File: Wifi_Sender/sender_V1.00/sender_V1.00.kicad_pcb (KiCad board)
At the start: 2 copper layers, 2 parts, among them U1 ESP32-DevKitC, U2 Teensy4.1

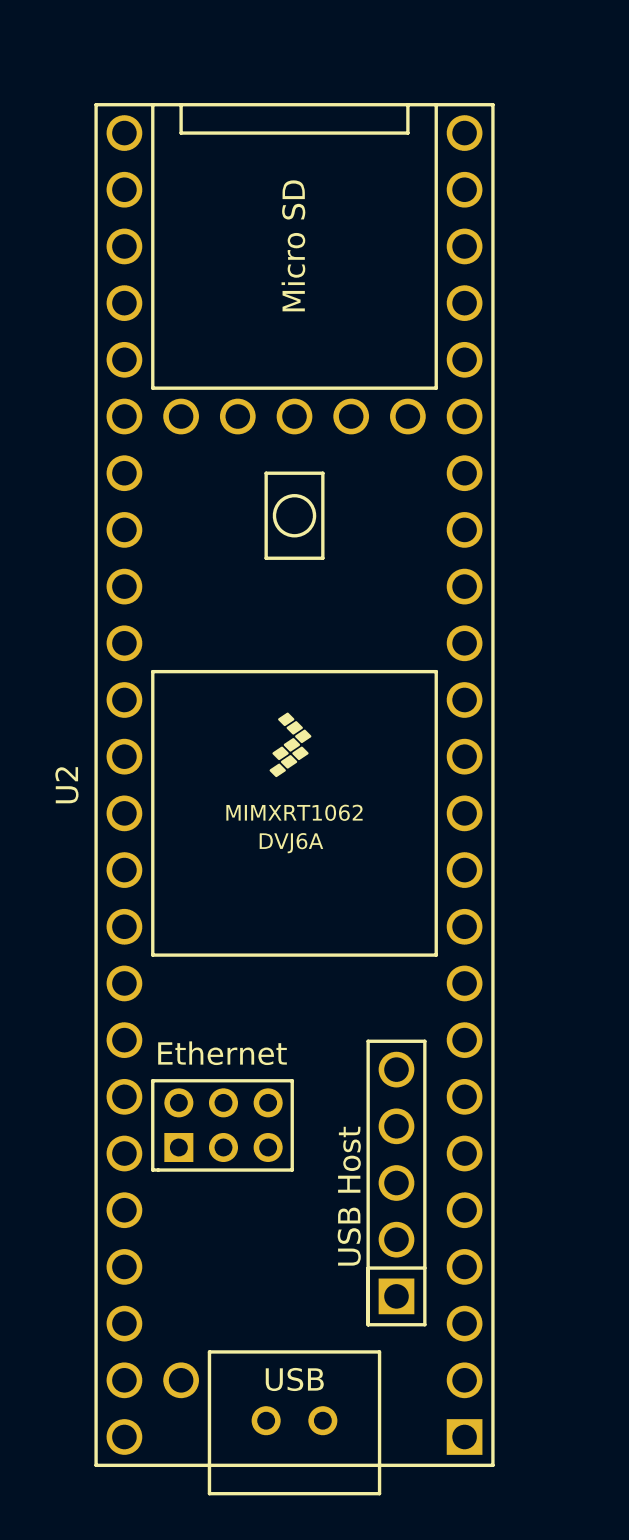
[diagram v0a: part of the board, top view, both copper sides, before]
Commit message: Removed old Pics
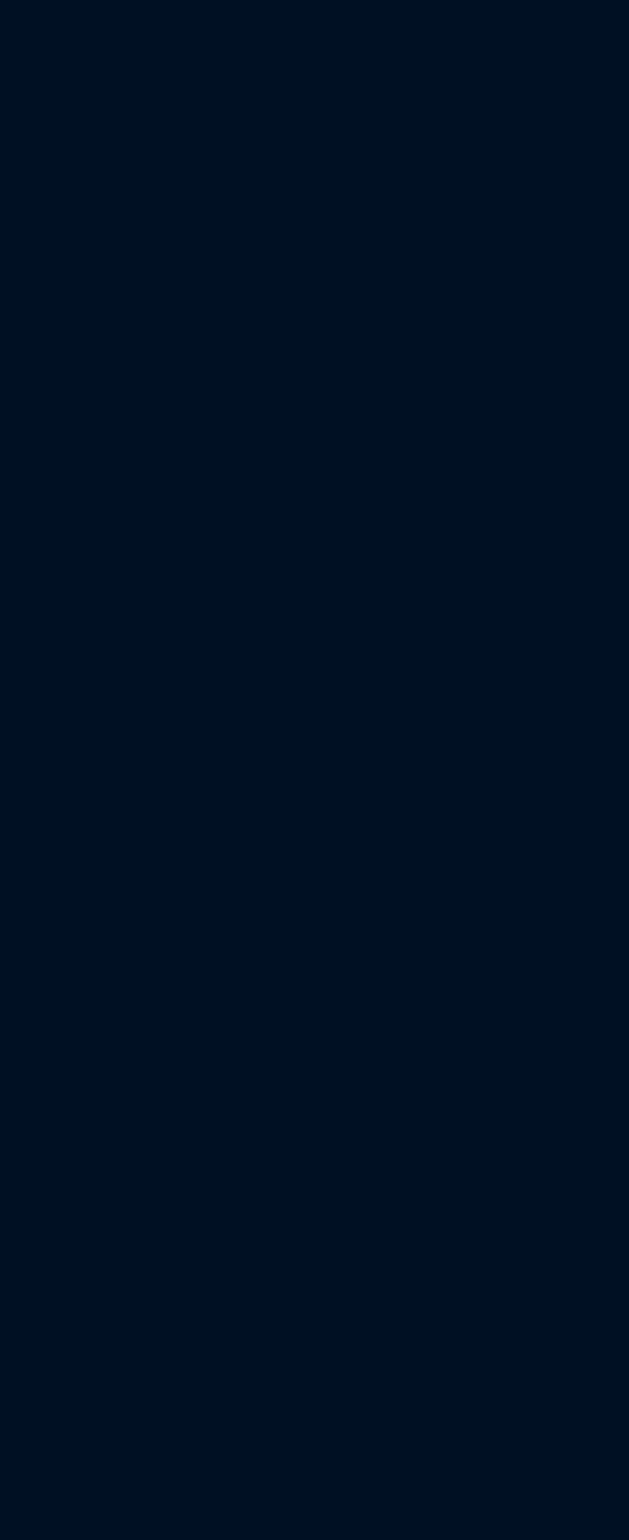
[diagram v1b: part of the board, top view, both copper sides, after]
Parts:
- removed U2: Teensy4.1, teensy:Teensy41
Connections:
- U1 pad 1: Net-(U1-Pad1) -> unconnected-(U1-Pad1)
- U1 pad 10: Net-(U1-Pad10) -> unconnected-(U1-Pad10)
- U1 pad 11: Net-(U1-Pad11) -> unconnected-(U1-Pad11)
- U1 pad 12: Net-(U1-Pad12) -> unconnected-(U1-Pad12)
- U1 pad 13: Net-(U1-Pad13) -> unconnected-(U1-Pad13)
- U1 pad 14: Net-(U1-Pad14) -> unconnected-(U1-Pad14)
- U1 pad 15: Net-(U1-Pad15) -> unconnected-(U1-Pad15)
- U1 pad 16: Net-(U1-Pad16) -> unconnected-(U1-Pad16)
- U1 pad 17: Net-(U1-Pad17) -> unconnected-(U1-Pad17)
- U1 pad 18: Net-(U1-Pad18) -> unconnected-(U1-Pad18)
- U1 pad 19: Net-(U1-Pad19) -> unconnected-(U1-Pad19)
- U1 pad 2: Net-(U1-Pad2) -> unconnected-(U1-Pad2)
- U1 pad 20: Net-(U1-Pad20) -> unconnected-(U1-Pad20)
- U1 pad 21: Net-(U1-Pad21) -> unconnected-(U1-Pad21)
- U1 pad 22: Net-(U1-Pad22) -> unconnected-(U1-Pad22)
- U1 pad 23: Net-(U1-Pad23) -> unconnected-(U1-Pad23)
- U1 pad 24: Net-(U1-Pad24) -> unconnected-(U1-Pad24)
- U1 pad 25: Net-(U1-Pad25) -> unconnected-(U1-Pad25)
- U1 pad 26: Net-(U1-Pad26) -> unconnected-(U1-Pad26)
- U1 pad 27: Net-(U1-Pad27) -> unconnected-(U1-Pad27)
- U1 pad 28: Net-(U1-Pad28) -> unconnected-(U1-Pad28)
- U1 pad 29: Net-(U1-Pad29) -> unconnected-(U1-Pad29)
- U1 pad 3: Net-(U1-Pad3) -> unconnected-(U1-Pad3)
- U1 pad 30: Net-(U1-Pad30) -> unconnected-(U1-Pad30)
- U1 pad 31: Net-(U1-Pad31) -> unconnected-(U1-Pad31)
- U1 pad 32: Net-(U1-Pad32) -> unconnected-(U1-Pad32)
- U1 pad 33: Net-(U1-Pad33) -> unconnected-(U1-Pad33)
- U1 pad 34: Net-(U1-Pad34) -> unconnected-(U1-Pad34)
- U1 pad 35: Net-(U1-Pad35) -> unconnected-(U1-Pad35)
- U1 pad 36: Net-(U1-Pad36) -> unconnected-(U1-Pad36)
- U1 pad 37: Net-(U1-Pad37) -> unconnected-(U1-Pad37)
- U1 pad 38: Net-(U1-Pad38) -> unconnected-(U1-Pad38)
- U1 pad 4: Net-(U1-Pad4) -> unconnected-(U1-Pad4)
- U1 pad 5: Net-(U1-Pad5) -> unconnected-(U1-Pad5)
- U1 pad 6: Net-(U1-Pad6) -> unconnected-(U1-Pad6)
- U1 pad 7: Net-(U1-Pad7) -> unconnected-(U1-Pad7)
- U1 pad 8: Net-(U1-Pad8) -> unconnected-(U1-Pad8)
- U1 pad 9: Net-(U1-Pad9) -> unconnected-(U1-Pad9)
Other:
- net class Default removed

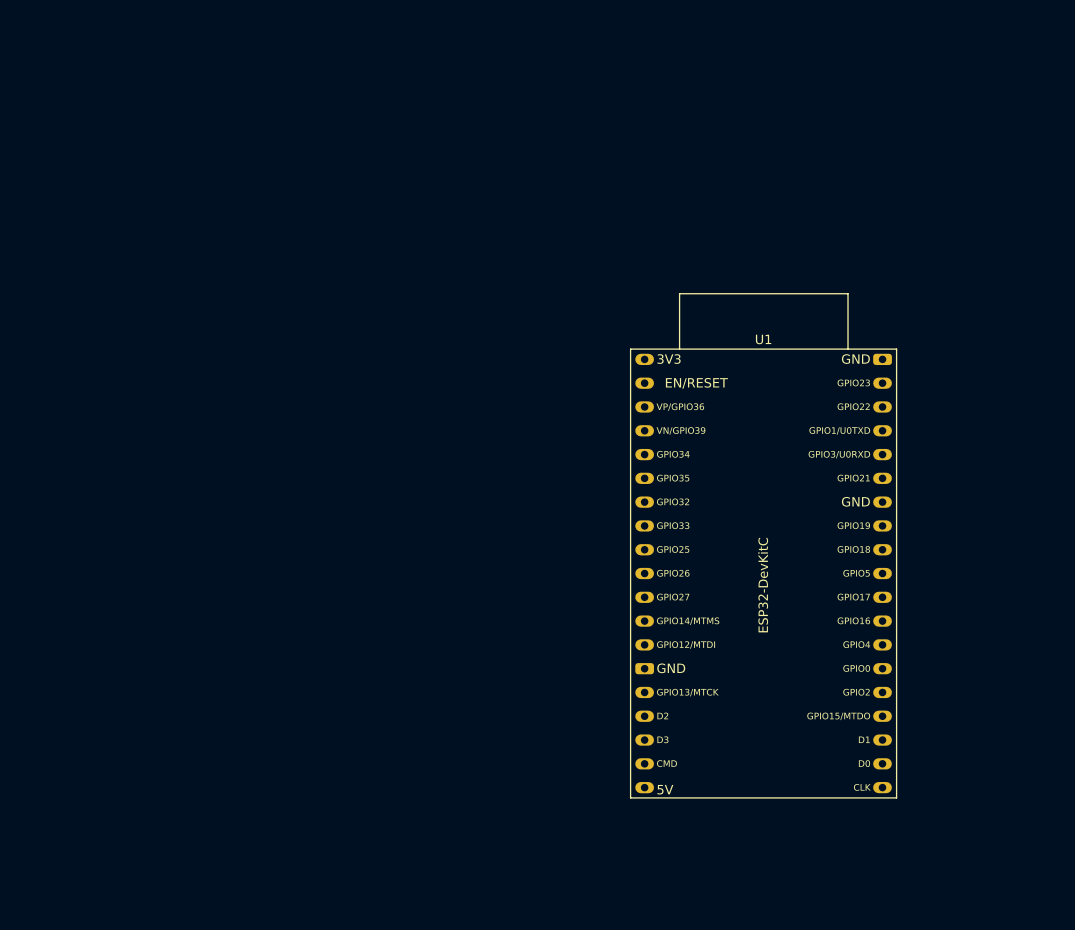
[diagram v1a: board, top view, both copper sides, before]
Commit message: Start Design of Sender
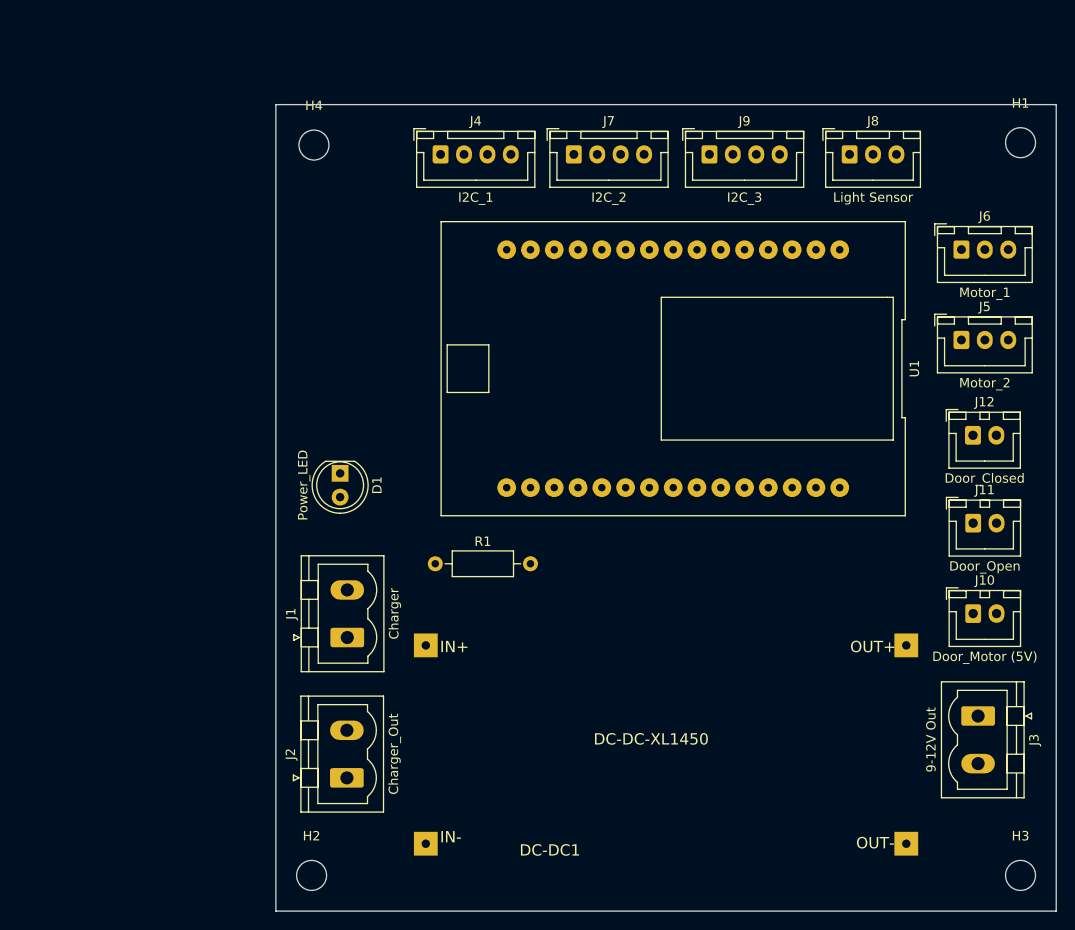
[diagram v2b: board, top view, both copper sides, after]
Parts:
- added D1: Power_LED, LED_THT:LED_D5.0mm, F.Cu at (68.1, 60.7)
- added DC-DC1: DC-DC-XL1450, Zimprich:DCDC-XL1450, F.Cu at (94.8, 91.6)
- added H1: MountingHole, MountingHole:MountingHole_3.2mm_M3, F.Cu at (140.7, 25.4)
- added H2: MountingHole, MountingHole:MountingHole_3.2mm_M3, F.Cu at (65.0, 103.6)
- added H3: MountingHole, MountingHole:MountingHole_3.2mm_M3, F.Cu at (140.7, 103.6)
- added H4: MountingHole, MountingHole:MountingHole_3.2mm_M3, F.Cu at (65.3, 25.7)
- added J1: Charger, Connector_Phoenix_MSTB:PhoenixContact_MSTBVA_2,5_2-G-5,08_1x02_P5.08mm_Vertical, F.Cu at (68.8, 78.2)
- added J10: Door_Motor (5V), Connector_JST:JST_XH_B2B-XH-A_1x02_P2.50mm_Vertical, F.Cu at (135.7, 75.7)
- added J11: Door_Open, Connector_JST:JST_XH_B2B-XH-A_1x02_P2.50mm_Vertical, F.Cu at (135.7, 66.0)
- added J12: Door_Closed, Connector_JST:JST_XH_B2B-XH-A_1x02_P2.50mm_Vertical, F.Cu at (135.6, 56.6)
- added J2: Charger_Out, Connector_Phoenix_MSTB:PhoenixContact_MSTBVA_2,5_2-G-5,08_1x02_P5.08mm_Vertical, F.Cu at (68.8, 93.2)
- added J3: 9-12V Out, Connector_Phoenix_MSTB:PhoenixContact_MSTBVA_2,5_2-G-5,08_1x02_P5.08mm_Vertical, F.Cu at (136.2, 86.6)
- added J4: I2C_1, Connector_JST:JST_XH_B4B-XH-A_1x04_P2.50mm_Vertical, F.Cu at (78.8, 26.7)
- added J5: Motor_2, Connector_JST:JST_XH_B3B-XH-A_1x03_P2.50mm_Vertical, F.Cu at (134.4, 46.5)
- added J6: Motor_1, Connector_JST:JST_XH_B3B-XH-A_1x03_P2.50mm_Vertical, F.Cu at (134.4, 36.8)
- added J7: I2C_2, Connector_JST:JST_XH_B4B-XH-A_1x04_P2.50mm_Vertical, F.Cu at (93.0, 26.7)
- added J8: Light Sensor, Connector_JST:JST_XH_B3B-XH-A_1x03_P2.50mm_Vertical, F.Cu at (122.5, 26.7)
- added J9: I2C_3, Connector_JST:JST_XH_B4B-XH-A_1x04_P2.50mm_Vertical, F.Cu at (107.5, 26.7)
- added R1: 220, Resistor_THT:R_Axial_DIN0207_L6.3mm_D2.5mm_P10.16mm_Horizontal, F.Cu at (78.2, 70.4)
- U1: value ESP32-DevKitC -> ESP32-DEVKIT-V1; footprint Espressif:ESP32-DevKitC -> teensy_library-master:ESP32-DEVKIT-V1
- moved U1 3.21 mm to (103.6, 49.5), turned to 180 degrees
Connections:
- U1 pad 11: unconnected-(U1-Pad11) -> Input_3
- U1 pad 12: unconnected-(U1-Pad12) -> Input_1
- U1 pad 13: unconnected-(U1-Pad13) -> Input_2
- U1 pad 14: unconnected-(U1-Pad14) -> GND
- U1 pad 15: unconnected-(U1-Pad15) -> VCC
- U1 pad 16: unconnected-(U1-Pad16) -> +3V3
- U1 pad 17: unconnected-(U1-Pad17) -> GND
- U1 pad 18: unconnected-(U1-Pad18) -> SCL
- U1 pad 20: unconnected-(U1-Pad20) -> SDA
- U1 pad 24: unconnected-(U1-Pad24) -> Input_4
- U1 pad 25: unconnected-(U1-Pad25) -> Enable_B
- U1 pad 30: unconnected-(U1-Pad30) -> Enable_A
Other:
- board outline added: 83.3 x 86.1 mm

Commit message: Add Gerber Files
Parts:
- removed DC-DC1: DC-DC-XL1450, Zimprich:DCDC-XL1450
- removed J11: Door_Open, Connector_JST:JST_XH_B2B-XH-A_1x02_P2.50mm_Vertical
- removed J12: Door_Closed, Connector_JST:JST_XH_B2B-XH-A_1x02_P2.50mm_Vertical
- added SW1: PowerSwitch, Connector_PinHeader_2.54mm:PinHeader_1x02_P2.54mm_Vertical, F.Cu at (66.0, 41.9)
- J1: value Charger -> 9-12V In
- J10: value Door_Motor (5V) -> Door_Closed
- J2: value Charger_Out -> 9-12V Out
- J3: value 9-12V Out -> I2C_1; footprint Connector_Phoenix_MSTB:PhoenixContact_MSTBVA_2,5_2-G-5,08_1x02_P5.08mm_Vertical -> Connector_JST:JST_XH_B4B-XH-A_1x04_P2.50mm_Vertical
- J4: value I2C_1 -> Motor_2; footprint Connector_JST:JST_XH_B4B-XH-A_1x04_P2.50mm_Vertical -> Connector_JST:JST_XH_B3B-XH-A_1x03_P2.50mm_Vertical
- J5: value Motor_2 -> Motor_1
- J6: value Motor_1 -> I2C_2; footprint Connector_JST:JST_XH_B3B-XH-A_1x03_P2.50mm_Vertical -> Connector_JST:JST_XH_B4B-XH-A_1x04_P2.50mm_Vertical
- J7: value I2C_2 -> Light Sensor; footprint Connector_JST:JST_XH_B4B-XH-A_1x04_P2.50mm_Vertical -> Connector_JST:JST_XH_B3B-XH-A_1x03_P2.50mm_Vertical
- J8: value Light Sensor -> I2C_3; footprint Connector_JST:JST_XH_B3B-XH-A_1x03_P2.50mm_Vertical -> Connector_JST:JST_XH_B4B-XH-A_1x04_P2.50mm_Vertical
- J9: value I2C_3 -> Door_Open; footprint Connector_JST:JST_XH_B4B-XH-A_1x04_P2.50mm_Vertical -> Connector_JST:JST_XH_B2B-XH-A_1x02_P2.50mm_Vertical
- moved J2 75.2 mm to (139.2, 66.8), turned to 180 degrees
- moved J5 53.4 mm to (84.6, 27.2), turned to 180 degrees
- moved J10 50.5 mm to (127.0, 25.9)
- moved J3 49.5 mm to (140.5, 37.3), turned to 180 degrees
- moved R1 37.3 mm to (73.9, 33.3), turned to 90 degrees
- moved H3 36.7 mm to (124.2, 70.9)
- moved J8 35.0 mm to (140.5, 56.6), turned to 180 degrees
- moved H2 32.0 mm to (65.3, 71.6)
- moved D1 27.2 mm to (66.5, 33.5)
- moved J1 18.3 mm to (71.9, 60.2), turned to 180 degrees
- moved J4 18.2 mm to (97.0, 27.2), turned to 180 degrees
- moved J7 11.7 mm to (104.7, 25.9)
- moved J6 11.6 mm to (140.5, 46.7), turned to 180 degrees
- moved J9 9.64 mm to (117.1, 25.9)
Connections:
- J1 pad 1: Net-(DC-DC1-PadI-) -> Net-(J1-Pad1)
- J1 pad 2: Net-(DC-DC1-PadI+) -> GND
- J10 pad 1: unconnected-(J10-Pad1) -> GND
- J10 pad 2: unconnected-(J10-Pad2) -> Door_Closed
- J2 pad 1: Net-(DC-DC1-PadI-) -> Net-(J2-Pad1)
- J2 pad 2: Net-(DC-DC1-PadI+) -> GND
- J3 pad 1: VCC -> SDA
- J3 pad 2: GND -> SCL
- J4 pad 1: SDA -> Enable_B
- J4 pad 2: SCL -> Input_4
- J4 pad 3: GND -> Input_3
- J5 pad 1: Enable_B -> Enable_A
- J5 pad 2: Input_4 -> Input_1
- J5 pad 3: Input_3 -> Input_2
- J6 pad 1: Enable_A -> SDA
- J6 pad 2: Input_1 -> SCL
- J6 pad 3: Input_2 -> GND
- J7 pad 1: SDA -> +3V3
- J7 pad 2: SCL -> GND
- J7 pad 3: GND -> D0
- J8 pad 1: +3V3 -> SDA
- J8 pad 2: GND -> SCL
- J8 pad 3: D0 -> GND
- J9 pad 1: SDA -> GND
- J9 pad 2: SCL -> Door_Open
- R1 pad 2: Power_LED -> +3V3
- U1 pad 15: VCC -> Net-(J2-Pad1)
- U1 pad 5: unconnected-(U1-Pad5) -> D0
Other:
- board size 83.3 x 86.1 mm -> 83.3 x 54.9 mm

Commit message: Update
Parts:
- removed D1: Power_LED, LED_THT:LED_D5.0mm
- added DC-DC1: DC-DC-XL1450, Zimprich:DCDC-XL1450, F.Cu at (50.8, 61.0)
- added J11: Door_Closed, Connector_JST:JST_XH_B2B-XH-A_1x02_P2.50mm_Vertical, F.Cu at (103.9, 17.5)
- added J12: 5V IN, Connector_JST:JST_XH_B2B-XH-A_1x02_P2.50mm_Vertical, F.Cu at (124.5, 75.9)
- added J13: I2C_3, Connector_JST:JST_XH_B4B-XH-A_1x04_P2.50mm_Vertical, F.Cu at (85.1, 17.6)
- added R2: 220, Resistor_THT:R_Axial_DIN0207_L6.3mm_D2.5mm_P10.16mm_Horizontal, F.Cu at (122.2, 51.8)
- added U2: ESP32-DEVKIT-V1, teensy_library-master:ESP32-DEVKIT-V1, F.Cu at (103.1, 55.1)
- added U3: INA226-Sense_I2C, Current_sense:INA226, F.Cu at (72.6, 65.0)
- added kibuzzard-63696024: G***, kibuzzard-63696024, F.Cu at (37.3, 55.4)
- J1: value 9-12V In -> Charger
- J10: value Door_Closed -> Door_Open
- J2: value 9-12V Out -> Charge Out
- J3: value I2C_1 -> Perimeter; footprint Connector_JST:JST_XH_B4B-XH-A_1x04_P2.50mm_Vertical -> Connector_Phoenix_MSTB:PhoenixContact_MSTBVA_2,5_2-G-5,08_1x02_P5.08mm_Vertical
- J4: value Motor_2 -> I2C_1; footprint Connector_JST:JST_XH_B3B-XH-A_1x03_P2.50mm_Vertical -> Connector_JST:JST_XH_B4B-XH-A_1x04_P2.50mm_Vertical
- J5: value Motor_1 -> Motor_2
- J6: value I2C_2 -> Motor_1; footprint Connector_JST:JST_XH_B4B-XH-A_1x04_P2.50mm_Vertical -> Connector_JST:JST_XH_B3B-XH-A_1x03_P2.50mm_Vertical
- J7: value Light Sensor -> I2C_2; footprint Connector_JST:JST_XH_B3B-XH-A_1x03_P2.50mm_Vertical -> Connector_JST:JST_XH_B4B-XH-A_1x04_P2.50mm_Vertical
- J8: value I2C_3 -> Light Sensor; footprint Connector_JST:JST_XH_B4B-XH-A_1x04_P2.50mm_Vertical -> Connector_JST:JST_XH_B3B-XH-A_1x03_P2.50mm_Vertical
- J9: value Door_Open -> Green_Red_Led; footprint Connector_JST:JST_XH_B2B-XH-A_1x02_P2.50mm_Vertical -> Connector_JST:JST_XH_B3B-XH-A_1x03_P2.50mm_Vertical
- R1: value 220 -> 2K2
- U1: value ESP32-DEVKIT-V1 -> INA226-Sense_I2C; footprint teensy_library-master:ESP32-DEVKIT-V1 -> Current_sense:INA226
- moved J2 102.6 mm to (48.0, 19.8), turned to 0 degrees
- moved J3 81.7 mm to (74.9, 86.1)
- moved J5 67.6 mm to (115.8, 87.1)
- moved H1 64.9 mm to (125.0, 88.4)
- moved J6 60.5 mm to (95.2, 86.9)
- moved J8 59.4 mm to (95.8, 17.6), turned to -90 degrees
- moved R1 56.0 mm to (126.7, 51.8)
- moved H3 53.1 mm to (126.0, 17.8)
- moved SW1 48.0 mm to (61.2, 89.7), turned to 180 degrees
- moved J9 32.1 mm to (125.2, 56.9), turned to -90 degrees
- moved J1 31.7 mm to (53.3, 85.9)
- moved H2 31.4 mm to (38.6, 88.1)
- moved U1 31.1 mm to (73.7, 41.1), turned to 90 degrees
- moved J4 30.8 mm to (66.3, 25.1), turned to 90 degrees
- moved J7 29.4 mm to (76.5, 17.6), turned to -90 degrees
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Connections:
- J10 pad 2: Door_Closed -> Door_Open
- J3 pad 1: SDA -> Net-(J3-Pad1)
- J3 pad 2: SCL -> GND
- J4 pad 1: Enable_B -> SDA
- J4 pad 2: Input_4 -> SCL
- J4 pad 3: Input_3 -> GND
- J5 pad 1: Enable_A -> Enable_B
- J5 pad 2: Input_1 -> Input_4
- J5 pad 3: Input_2 -> Input_3
- J6 pad 1: SDA -> Enable_A
- J6 pad 2: SCL -> Input_1
- J6 pad 3: GND -> Input_2
- J7 pad 1: +3V3 -> SDA
- J7 pad 2: GND -> SCL
- J7 pad 3: D0 -> GND
- J8 pad 1: SDA -> +3V3
- J8 pad 2: SCL -> GND
- J8 pad 3: GND -> D0
- J9 pad 2: Door_Open -> Net-(J9-Pad2)
- R1 pad 1: Net-(D1-Pad2) -> Net-(J9-Pad2)
- R1 pad 2: +3V3 -> RED
- SW1 pad 2: Net-(J2-Pad1) -> Net-(DC-DC1-PadI+)
- U1 pad 10: unconnected-(U1-Pad10) -> Net-(J2-Pad1)
- U1 pad 3: unconnected-(U1-Pad3) -> Net-(DC-DC1-PadI+)
- U1 pad 5: D0 -> SCL
- U1 pad 6: unconnected-(U1-Pad6) -> SDA
- U1 pad 7: unconnected-(U1-Pad7) -> GND
- U1 pad 8: unconnected-(U1-Pad8) -> +3V3
- U1 pad 9: unconnected-(U1-Pad9) -> Net-(DC-DC1-PadI+)
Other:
- board size 83.3 x 54.9 mm -> 96.3 x 80.5 mm
